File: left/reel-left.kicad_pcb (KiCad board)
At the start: 2 copper layers, 143.2 x 92.7 mm, 49 parts, among them J1 Conn_01x02, SW1 SW_Push, SW10 SW_Push, SW11 SW_Push, SW12 SW_Push, SW13 SW_Push, SW14 SW_Push, SW15 SW_Push, SW16 SW_Push, SW17 SW_Push, SW18 SW_Push, SW19 SW_Push, SW2 SW_Push, SW20 SW_Push, SW21 RotaryEncoder, SW22 SW_SPDT, SW3 SW_Push, SW4 SW_Push, SW5 SW_Push, SW6 SW_Push, SW7 SW_Push, SW8 SW_Push, SW9 SW_Push, U1 XIAO-nRF52840-Plus-SMD

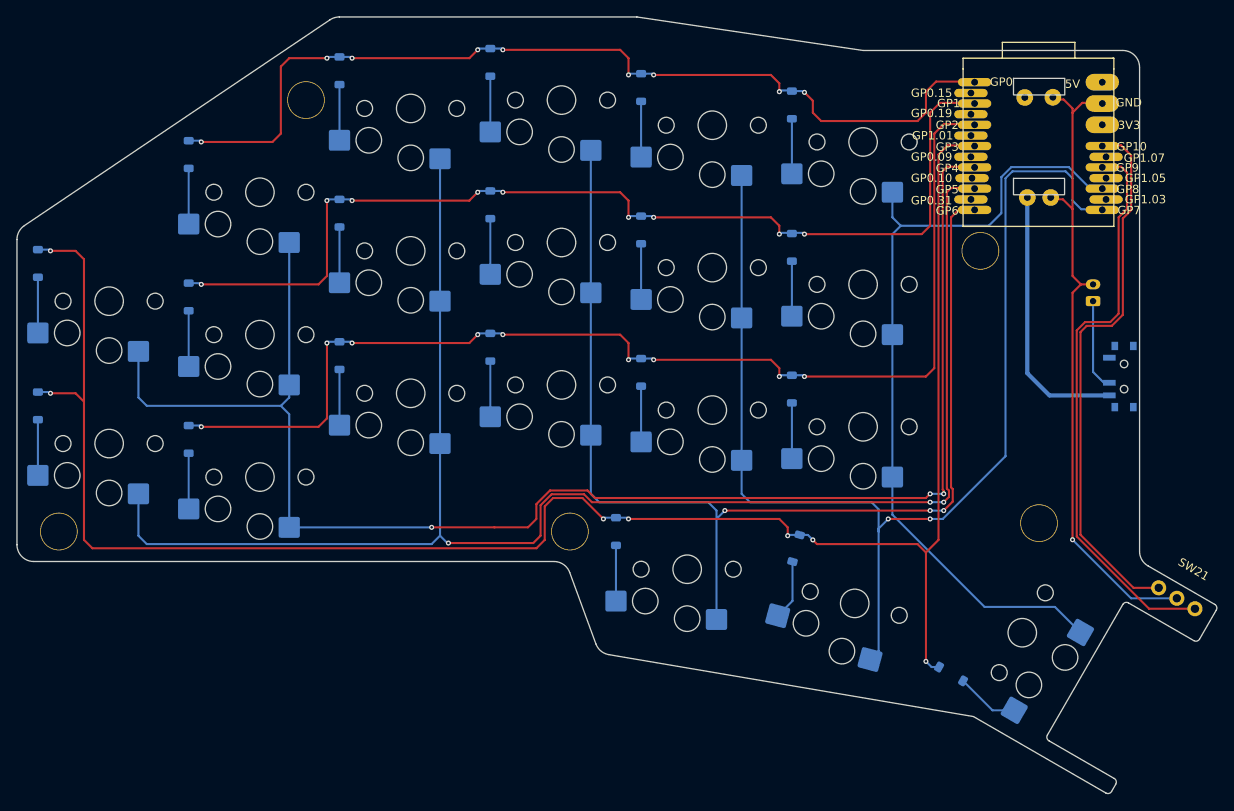
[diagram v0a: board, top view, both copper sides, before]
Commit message: Update XIAO BLE footprints
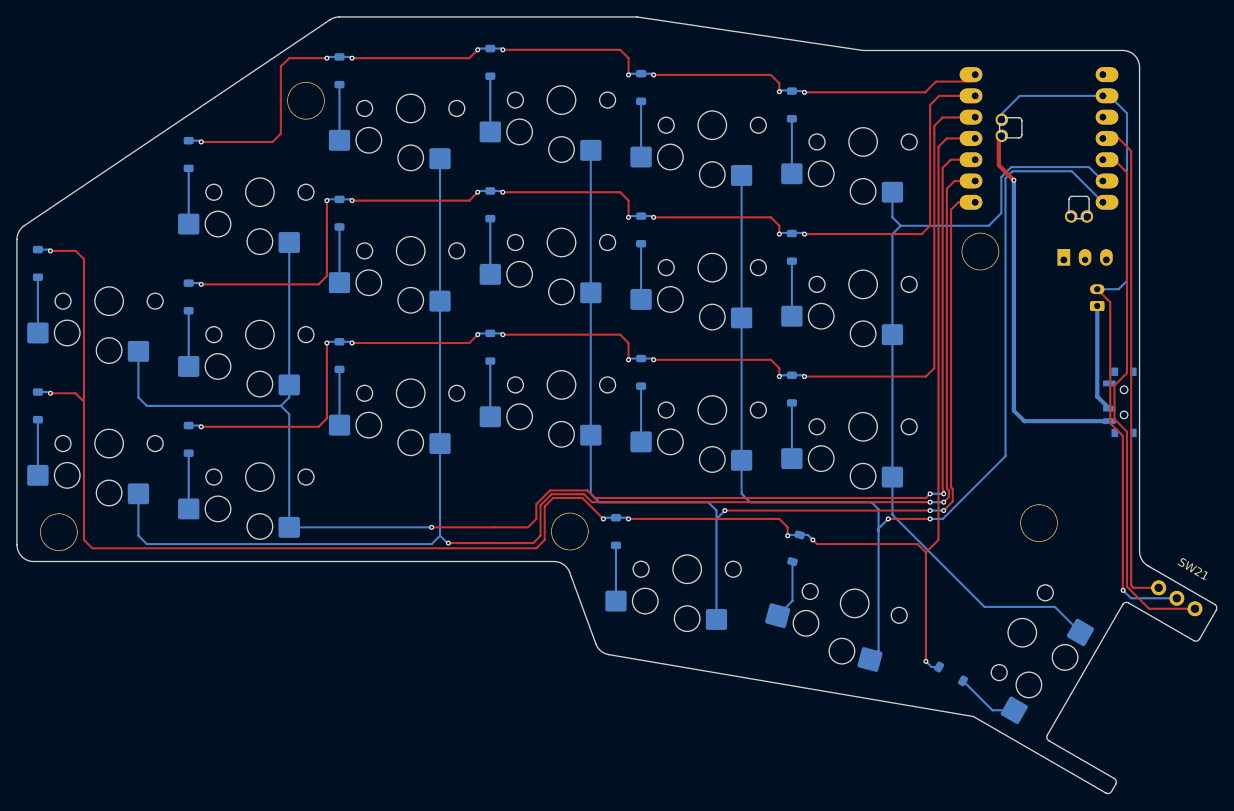
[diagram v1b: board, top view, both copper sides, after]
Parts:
- U1: value XIAO-nRF52840-Plus-SMD -> ~; footprint reel:XIAO_nRF52840_plus_mki -> reel:XIAO_nRF52840_wBAT_wNFC_1
- moved U1 8.00 mm to (198.5, 57.0)
- moved SW22 3.08 mm to (208.3, 99.0)
- moved J1 0.76 mm to (205.4, 87.5)
- moved Ref** 0.08 mm to (191.5, 81.0)
- moved Ref** 0.08 mm to (81.5, 114.5)
- moved Ref** 0.08 mm to (111.0, 63.0)
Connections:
- U1 pad 15: GND -> unconnected-(U1-NFC1_0.09-Pad15)
- U1 pad 16: VBAT_SW -> unconnected-(U1-NFC2_0.10-Pad16)
- U1 pad 20: unconnected-(U1-GPIO_0.09-Pad20) -> VBAT_SW
- U1 pad 21: unconnected-(U1-GPIO_0.10-Pad21) -> GND
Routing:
- net VBAT_SW: track 31.5 -> 45.1 mm, vias 0 -> 1
- net RotA: track 65.4 -> 59.3 mm
- net GND: track 79.0 -> 85.0 mm
- net RotB: track 68.6 -> 63.4 mm
- net Row0: track 113.1 -> 108.0 mm
- net Net-(J1-Pin_1): track 10.9 -> 13.0 mm
- net Col3: track 141.1 -> 139.2 mm
- net Row3: track 222.4 -> 223.4 mm
- net Row2: track 136.9 -> 137.9 mm
- net Row1: track 122.4 -> 123.4 mm
- net Col2: track 136.1 -> 137.1 mm
- net Col1: track 193.1 -> 193.8 mm
- net Col0: track 182.0 -> 182.7 mm
- net unconnected-(SW22-A-Pad1): track 0.00 -> 0.65 mm
